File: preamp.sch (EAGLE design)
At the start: 19 parts, among them Q1 SST201, Q2 SST201, Q3 SST201

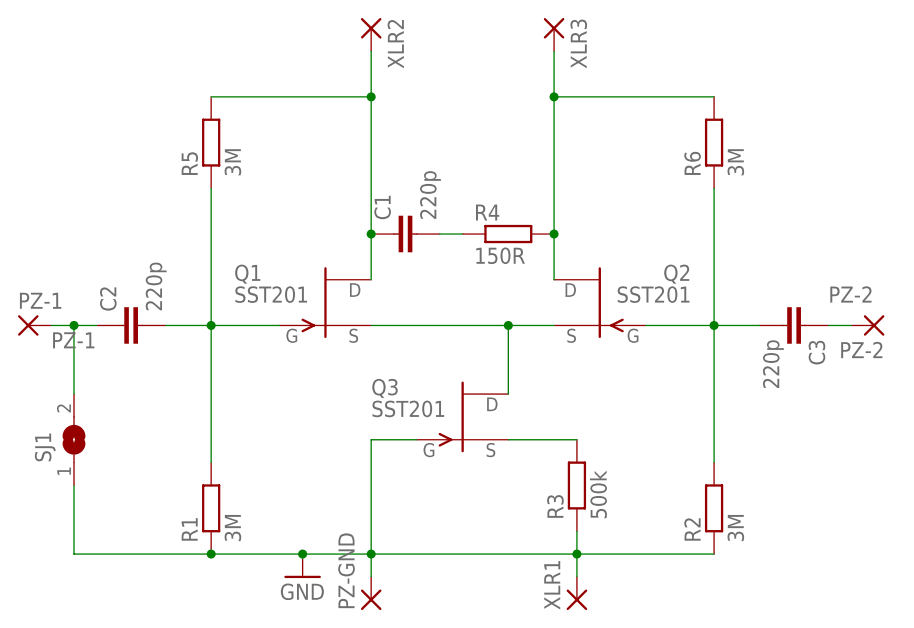
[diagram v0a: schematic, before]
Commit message: Change gain resistor to match IRL, add TODO notes
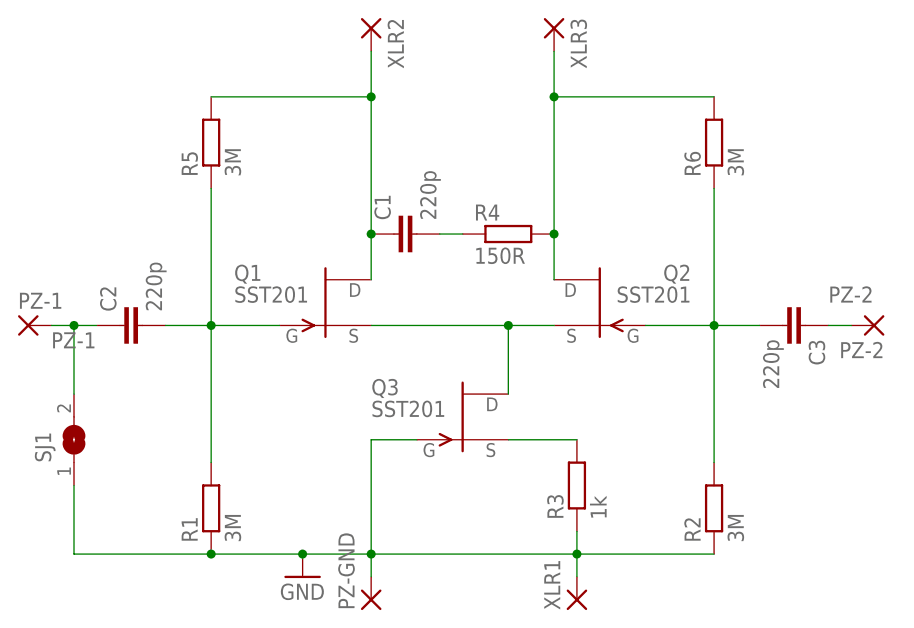
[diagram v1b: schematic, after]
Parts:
- R3: value 500k -> 1k
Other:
- note added: "PZ-1, PZ-2, PZ-GND: Change to TRS"
- note added: "R3: Add trimpot for trimmable gain"
- note added: "SJ1: Change to panel switch"
- note added: "XLR1, XLR2, XLR3: Change to XLR"
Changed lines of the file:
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@@
 <?xml version="1.0" encoding="utf-8"?>
 <!DOCTYPE eagle SYSTEM "eagle.dtd">
-<eagle version="9.2.2">
+<eagle version="9.2.1">
 <drawing>
 <settings>
@@
 <layer number="97" name="Info" color="7" fill="1" visible="yes" active="yes"/>
 <layer number="98" name="Guide" color="6" fill="1" visible="yes" active="yes"/>
+<layer number="100" name="TODO" color="13" fill="1" visible="yes" active="yes"/>
 </layers>
 <schematic xreflabel="%F%N/%S.%C%R" xrefpart="/%S.%C%R">
@@
 <part name="R1" library="rcl" deviceset="R-EU_" device="R1206" value="3M"/>
 <part name="R2" library="rcl" deviceset="R-EU_" device="R1206" value="3M"/>
-<part name="R3" library="rcl" deviceset="R-EU_" device="R1206" value="500k"/>
+<part name="R3" library="rcl" deviceset="R-EU_" device="R1206" value="1k"/>
 <part name="R4" library="rcl" deviceset="R-EU_" device="R1206" value="150R"/>
 <part name="C1" library="rcl" deviceset="C-EU" device="C1206" value="220p"/>
@@
 <sheet>
 <plain>
+<text x="68.58" y="27.94" size="1.778" layer="100">R3: Add trimpot
+for trimmable gain</text>
+<text x="10.16" y="15.24" size="1.778" layer="100">SJ1: Change to
+panel switch</text>
+<text x="40.64" y="0" size="1.778" layer="100">PZ-1, PZ-2, PZ-GND:
+Change to TRS</text>
+<text x="25.4" y="66.04" size="1.778" layer="100">XLR1, XLR2, XLR3:
+Change to XLR</text>
 </plain>
 <instances>
@@
 </drawing>
 <compatibility>
+<note version="6.3" minversion="6.2.2" severity="warning">
+Since Version 6.2.2 text objects can contain more than one line,
+which will not be processed correctly with this version.
+</note>
 <note version="8.2" severity="warning">
 Since Version 8.2, EAGLE supports online libraries. The ids
